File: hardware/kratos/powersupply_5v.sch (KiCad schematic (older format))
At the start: 4 parts, among them U3 MIC29310-5.0

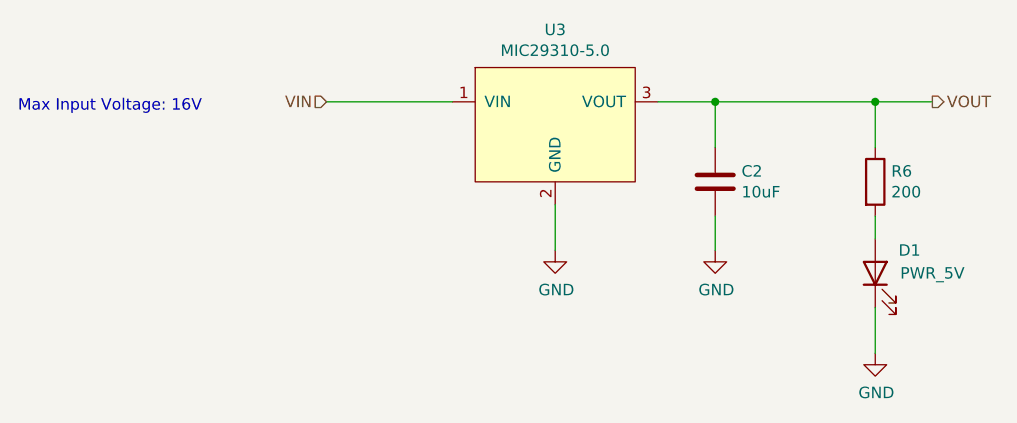
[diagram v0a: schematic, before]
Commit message: Update digikey part numbers in schematics
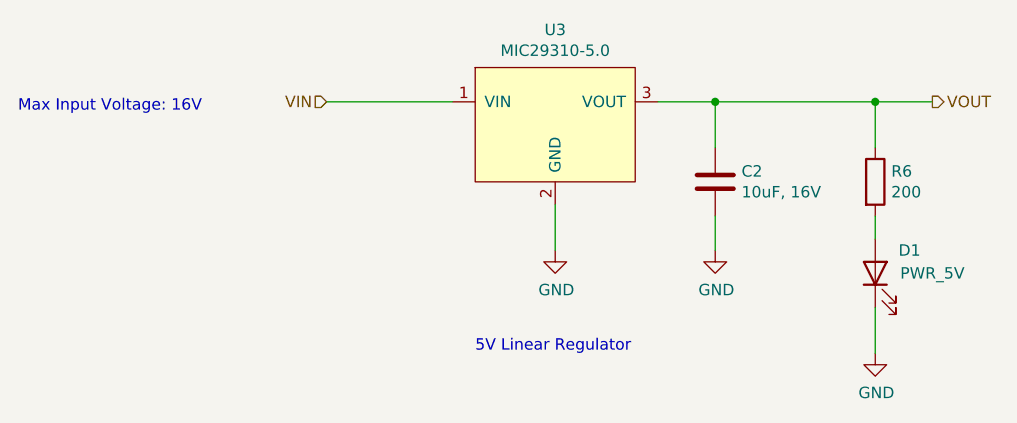
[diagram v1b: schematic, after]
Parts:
- C2: value 10uF -> 10uF, 16V; Digi-Key_PN (none) -> 511-1683-2-ND
- D1: Digi-Key_PN (none) -> 475-1410-2-ND
- R6: Digi-Key_PN (none) -> RMCF0805FT200RCT-ND
- U3: Digi-Key_PN (none) -> 576-2230-ND
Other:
- note added: "5V Linear Regulator"
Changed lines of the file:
@@
 F 2 "Package_TO_SOT_SMD:TO-263-3_TabPin2" H 5600 2650 50  0001 C CNN
 F 3 "https://ww1.microchip.com/downloads/en/DeviceDoc/mic29310.pdf" H 5450 3600 50  0001 C CNN
+F 4 "576-2230-ND" H 5600 3300 50  0001 C CNN "Digi-Key_PN"
 	1    5600 3300
 	1    0    0    -1
@@
 P 6300 3550
 F 0 "C2" H 6415 3596 50  0000 L CNN
-F 1 "10uF" H 6415 3505 50  0000 L CNN
+F 1 "10uF, 16V" H 6415 3505 50  0000 L CNN
 F 2 "Capacitor_SMD:C_0805_2012Metric" H 6338 3400 50  0001 C CNN
 F 3 "~" H 6300 3550 50  0001 C CNN
+F 4 "511-1683-2-ND" H 6300 3550 50  0001 C CNN "Digi-Key_PN"
 	1    6300 3550
 	1    0    0    -1
@@
 F 2 "LED_SMD:LED_0805_2012Metric" H 7000 3950 50  0001 C CNN
 F 3 "~" H 7000 3950 50  0001 C CNN
+F 4 "475-1410-2-ND" V 7000 3950 50  0001 C CNN "Digi-Key_PN"
 	1    7000 3950
 	0    -1   -1   0
@@
 F 2 "Resistor_SMD:R_0805_2012Metric" V 6930 3550 50  0001 C CNN
 F 3 "~" H 7000 3550 50  0001 C CNN
+F 4 "RMCF0805FT200RCT-ND" H 7000 3550 50  0001 C CNN "Digi-Key_PN"
 	1    7000 3550
 	1    0    0    -1
@@
 Wire Wire Line
 	7000 4100 7000 4300
+Text Notes 5250 4300 0    50   ~ 0
+5V Linear Regulator
 $EndSCHEMATC

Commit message: Update tantalum cap to polarized
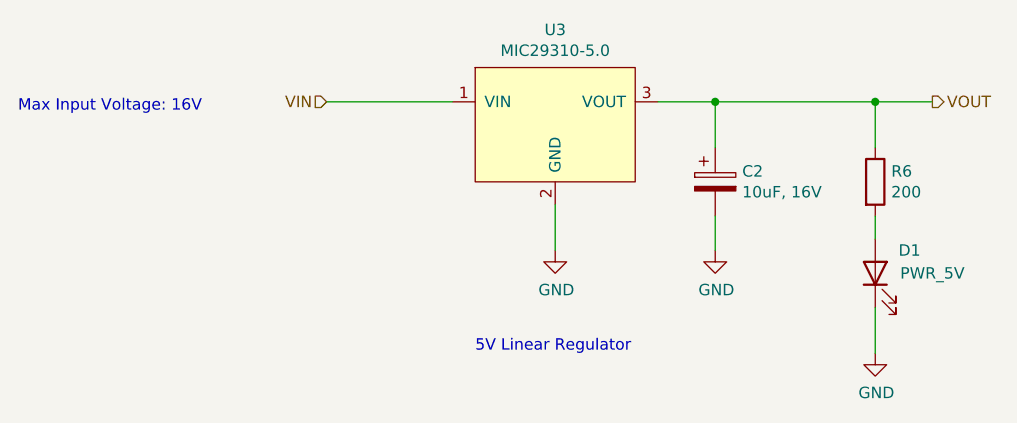
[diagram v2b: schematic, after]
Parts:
- removed C2: 10uF, 16V, Capacitor_SMD:C_0805_2012Metric, symbol Device:C
- added C2: 10uF, 16V, Capacitor_SMD:C_0805_2012Metric, symbol Device:CP
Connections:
- net GND: now also C2.2
- net VOUT: now also C2.1
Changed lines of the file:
@@
-	1    0    0    -1
-$EndComp
-$Comp
-L Device:C C2
-U 1 1 604EA0E2
-P 6300 3550
-F 0 "C2" H 6415 3596 50  0000 L CNN
-F 1 "10uF, 16V" H 6415 3505 50  0000 L CNN
-F 2 "Capacitor_SMD:C_0805_2012Metric" H 6338 3400 50  0001 C CNN
-F 3 "~" H 6300 3550 50  0001 C CNN
-F 4 "511-1683-2-ND" H 6300 3550 50  0001 C CNN "Digi-Key_PN"
-	1    6300 3550
 	1    0    0    -1
 $EndComp
@@
 Text Notes 5250 4300 0    50   ~ 0
 5V Linear Regulator
+$Comp
+L Device:CP C?
+U 1 1 60553334
+P 6300 3550
+AR Path="/604E226D/60553334" Ref="C?"  Part="1"
+AR Path="/604E6CA5/60553334" Ref="C2"  Part="1"
+F 0 "C2" H 6418 3596 50  0000 L CNN
+F 1 "10uF, 16V" H 6418 3505 50  0000 L CNN
+F 2 "Capacitor_SMD:C_0805_2012Metric" H 6338 3400 50  0001 C CNN
+F 3 "~" H 6300 3550 50  0001 C CNN
+F 4 "511-1683-2-ND" H 6300 3550 50  0001 C CNN "Digi-Key_PN"
+	1    6300 3550
+	1    0    0    -1
+$EndComp
 $EndSCHEMATC
